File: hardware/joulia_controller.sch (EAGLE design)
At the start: 41 parts, among them IC1 LM2902D, IC2 LM2902D, U1 MMBT2222ALT1G, U2 MMBT2222ALT1G

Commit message: Complete wiring with HV circuit and rearrangement
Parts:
- renumbered U$3 to HE_HEATSINK, U$4 to P_HEATSINK
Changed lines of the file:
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@@
 <part name="U$1" library="digikey" deviceset="T3050H-6I" device=""/>
 <part name="U$2" library="digikey" deviceset="T3050H-6I" device=""/>
-<part name="U$3" library="digikey" deviceset="VM1-038-1AE" device=""/>
-<part name="U$4" library="digikey" deviceset="VM1-038-1AE" device=""/>
+<part name="HE_HEATSINK" library="digikey" deviceset="VM1-038-1AE" device=""/>
+<part name="P_HEATSINK" library="digikey" deviceset="VM1-038-1AE" device=""/>
 <part name="U$5" library="digikey" deviceset="MOC3020S" device=""/>
 <part name="U$6" library="digikey" deviceset="MOC3020S" device=""/>
@@
 <instance part="U$1" gate="G$1" x="292.1" y="124.46"/>
 <instance part="U$2" gate="G$1" x="292.1" y="76.2"/>
-<instance part="U$3" gate="G$1" x="309.88" y="124.46"/>
-<instance part="U$4" gate="G$1" x="309.88" y="76.2"/>
+<instance part="HE_HEATSINK" gate="G$1" x="309.88" y="124.46"/>
+<instance part="P_HEATSINK" gate="G$1" x="309.88" y="76.2"/>
 <instance part="U$5" gate="G$1" x="256.54" y="121.92"/>
 <instance part="U$6" gate="G$1" x="256.54" y="73.66"/>

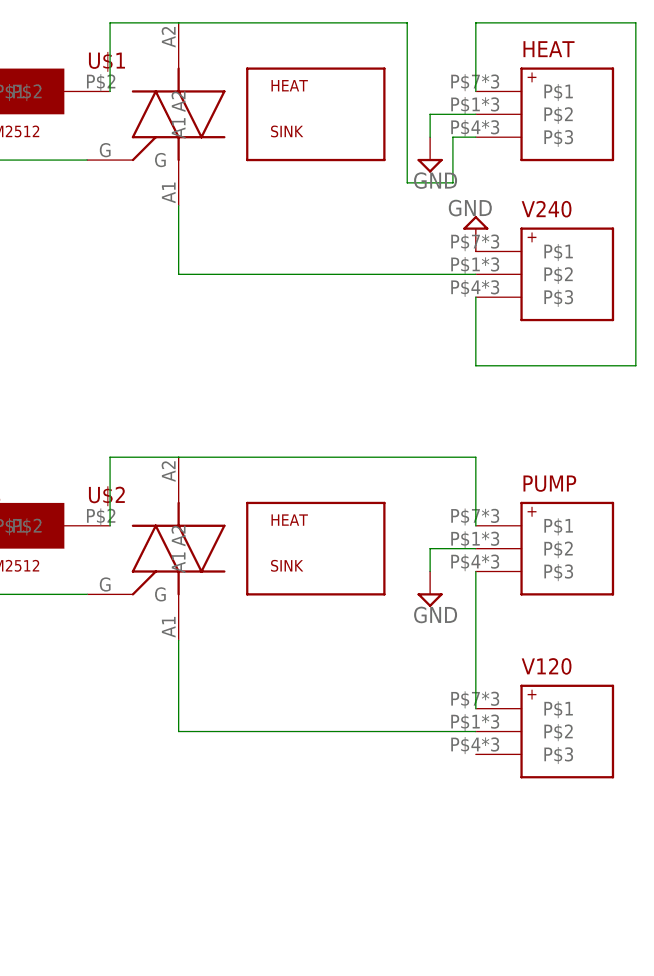
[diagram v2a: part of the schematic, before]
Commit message: Rewiring pump to be consistent with HE.
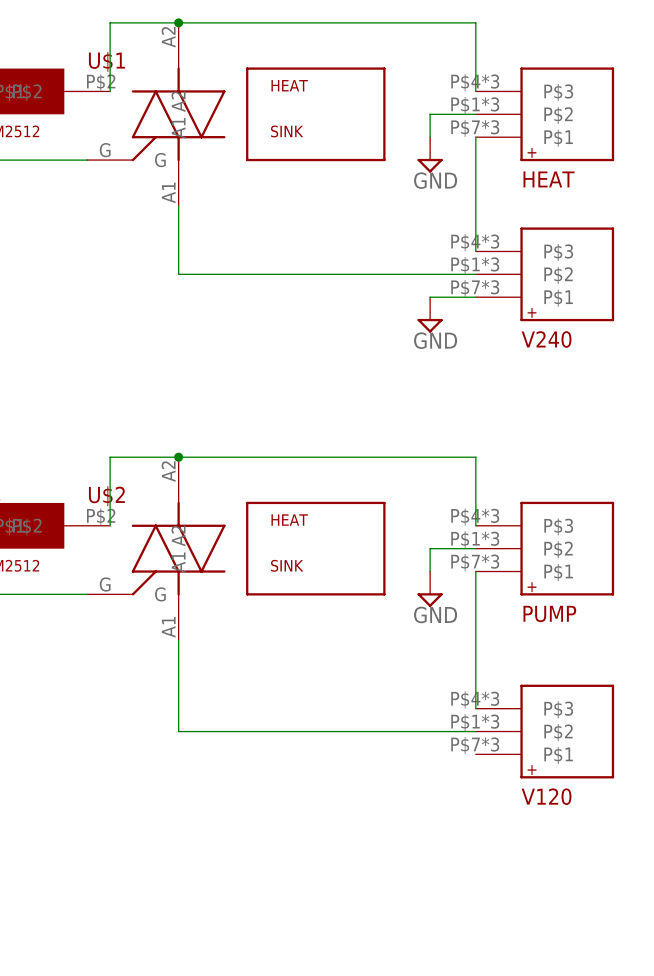
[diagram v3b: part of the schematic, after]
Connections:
- net N$26 renamed 120H
- net N$29 renamed +120
- net N$32 renamed -120
- removed net N$27: PUMP.P$3, V120.P$1
- new net 120N: PUMP.P$1, V120.P$3
- net N$24: now also PUMP.P$3; no longer PUMP.P$1
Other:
- moved on the sheet: HEAT, PUMP, V120, V240
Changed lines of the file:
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@@
 <instance part="P+1" gate="1" x="243.84" y="132.08"/>
 <instance part="P+2" gate="1" x="243.84" y="83.82"/>
-<instance part="HEAT" gate="G$1" x="332.74" y="124.46"/>
-<instance part="PUMP" gate="G$1" x="332.74" y="76.2"/>
+<instance part="HEAT" gate="G$1" x="332.74" y="124.46" rot="MR180"/>
+<instance part="PUMP" gate="G$1" x="332.74" y="76.2" rot="MR180"/>
 <instance part="SUPPLY17" gate="GND" x="322.58" y="119.38"/>
 <instance part="SUPPLY18" gate="GND" x="322.58" y="71.12"/>
-<instance part="V240" gate="G$1" x="332.74" y="106.68"/>
-<instance part="V120" gate="G$1" x="332.74" y="55.88"/>
-<instance part="SUPPLY19" gate="GND" x="327.66" y="111.76" rot="R180"/>
+<instance part="V240" gate="G$1" x="332.74" y="106.68" rot="MR180"/>
+<instance part="V120" gate="G$1" x="332.74" y="55.88" rot="MR180"/>
+<instance part="SUPPLY19" gate="GND" x="322.58" y="101.6"/>
 <instance part="R17" gate="G$1" x="243.84" y="111.76" rot="R90"/>
 <instance part="R18" gate="G$1" x="243.84" y="63.5" rot="R90"/>
@@
 <pinref part="V240" gate="G$1" pin="P$1"/>
 <pinref part="SUPPLY19" gate="GND" pin="GND"/>
+<wire x1="327.66" y1="104.14" x2="322.58" y2="104.14" width="0.1524" layer="91"/>
 </segment>
 </net>
@@
 <wire x1="287.02" y1="134.62" x2="294.64" y2="134.62" width="0.1524" layer="91"/>
 <pinref part="HEAT" gate="G$1" pin="P$3"/>
-<wire x1="327.66" y1="121.92" x2="325.12" y2="121.92" width="0.1524" layer="91"/>
-<wire x1="325.12" y1="121.92" x2="325.12" y2="116.84" width="0.1524" layer="91"/>
-<wire x1="325.12" y1="116.84" x2="320.04" y2="116.84" width="0.1524" layer="91"/>
-<wire x1="320.04" y1="116.84" x2="320.04" y2="134.62" width="0.1524" layer="91"/>
-<wire x1="320.04" y1="134.62" x2="294.64" y2="134.62" width="0.1524" layer="91"/>
+<wire x1="327.66" y1="127" x2="327.66" y2="134.62" width="0.1524" layer="91"/>
+<wire x1="327.66" y1="134.62" x2="294.64" y2="134.62" width="0.1524" layer="91"/>
+<junction x="294.64" y="134.62"/>
 </segment>
 </net>
@@
 <pinref part="U$2" gate="G$1" pin="A2"/>
 <wire x1="287.02" y1="86.36" x2="294.64" y2="86.36" width="0.1524" layer="91"/>
-<pinref part="PUMP" gate="G$1" pin="P$1"/>
-<wire x1="294.64" y1="86.36" x2="327.66" y2="86.36" width="0.1524" layer="91"/>
-<wire x1="327.66" y1="86.36" x2="327.66" y2="78.74" width="0.1524" layer="91"/>
-</segment>
-</net>
-<net name="N$26" class="1">
+<pinref part="PUMP" gate="G$1" pin="P$3"/>
+<wire x1="327.66" y1="78.74" x2="327.66" y2="86.36" width="0.1524" layer="91"/>
+<wire x1="327.66" y1="86.36" x2="294.64" y2="86.36" width="0.1524" layer="91"/>
+<junction x="294.64" y="86.36"/>
+</segment>
+</net>
+<net name="120H" class="1">
 <segment>
 <pinref part="U$2" gate="G$1" pin="A1"/>
@@
 </segment>
 </net>
-<net name="N$32" class="2">
+<net name="-120" class="2">
 <segment>
 <pinref part="V240" gate="G$1" pin="P$2"/>
@@
 </segment>
 </net>
-<net name="N$27" class="1">
-<segment>
-<pinref part="PUMP" gate="G$1" pin="P$3"/>
+<net name="+120" class="2">
+<segment>
+<pinref part="HEAT" gate="G$1" pin="P$1"/>
+<pinref part="V240" gate="G$1" pin="P$3"/>
+<wire x1="327.66" y1="121.92" x2="327.66" y2="109.22" width="0.1524" layer="91"/>
+</segment>
+</net>
+<net name="120N" class="1">
+<segment>
+<pinref part="PUMP" gate="G$1" pin="P$1"/>
+<pinref part="V120" gate="G$1" pin="P$3"/>
 <wire x1="327.66" y1="73.66" x2="327.66" y2="58.42" width="0.1524" layer="91"/>
-<pinref part="V120" gate="G$1" pin="P$1"/>
-</segment>
-</net>
-<net name="N$29" class="2">
-<segment>
-<pinref part="HEAT" gate="G$1" pin="P$1"/>
-<wire x1="327.66" y1="127" x2="327.66" y2="134.62" width="0.1524" layer="91"/>
-<wire x1="327.66" y1="134.62" x2="345.44" y2="134.62" width="0.1524" layer="91"/>
-<wire x1="345.44" y1="134.62" x2="345.44" y2="96.52" width="0.1524" layer="91"/>
-<pinref part="V240" gate="G$1" pin="P$3"/>
-<wire x1="345.44" y1="96.52" x2="327.66" y2="96.52" width="0.1524" layer="91"/>
-<wire x1="327.66" y1="96.52" x2="327.66" y2="104.14" width="0.1524" layer="91"/>
-</segment>
-</net>
+</segment>
+</net>

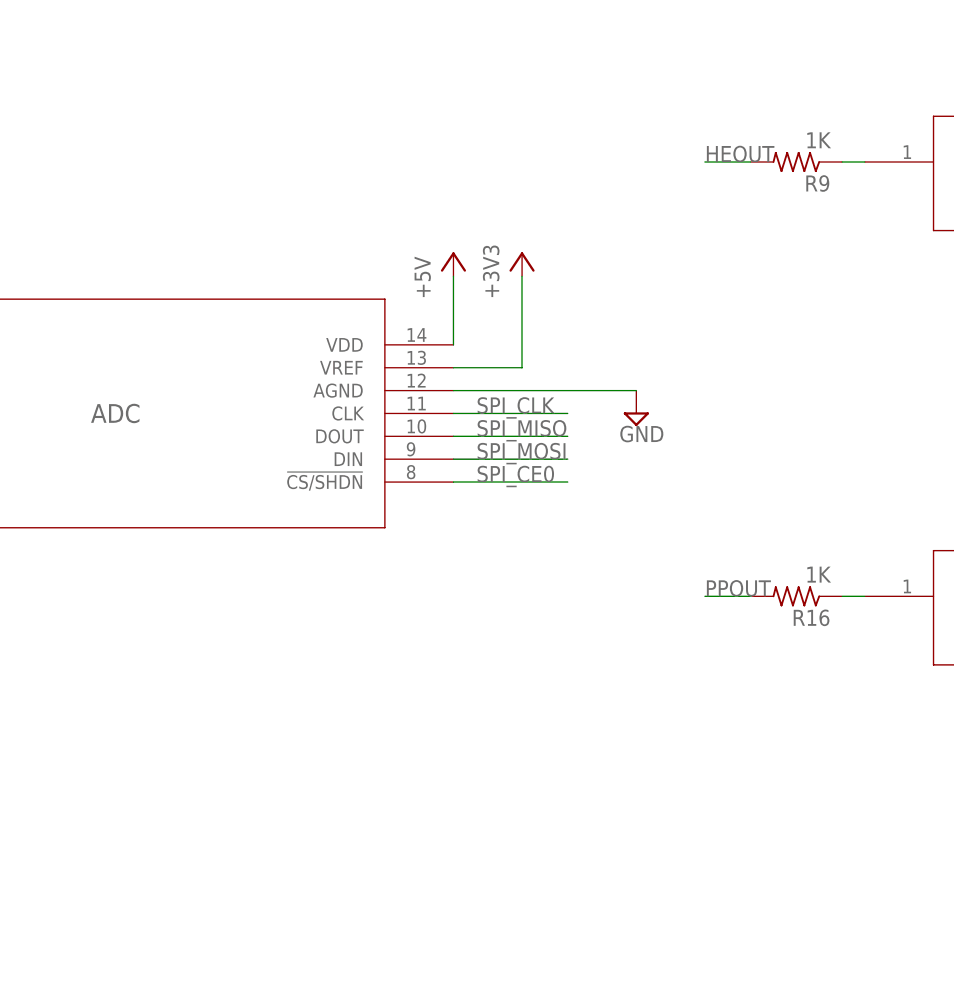
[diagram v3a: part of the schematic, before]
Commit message: Adding LEDs and Fan Connector
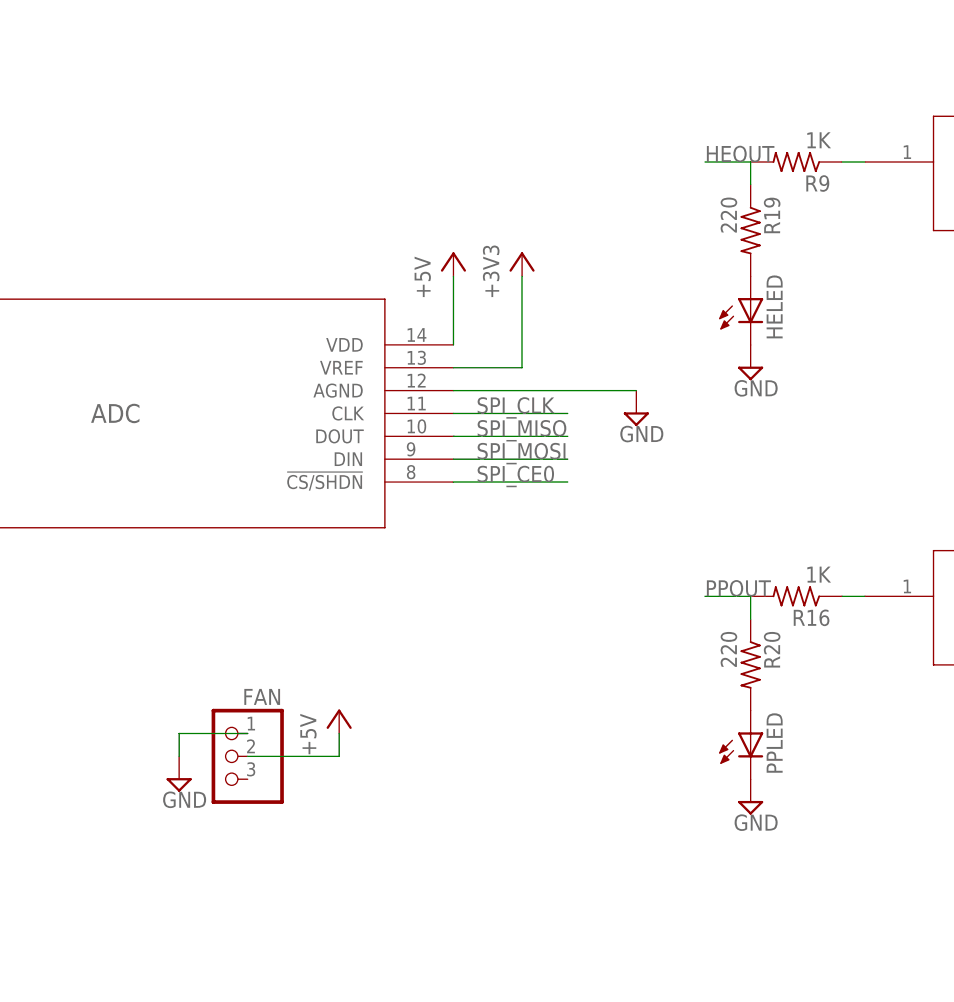
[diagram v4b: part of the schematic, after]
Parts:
- added FAN: (no value), adafruit:PINHD-1X3
- added HELED, PPLED: (no value), eagle-ltspice:LED_ESML0603
- added R19, R20: 220, rcl:R-US_R0402
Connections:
- new net N$25: HELED.A, R19.2
- new net N$26: PPLED.A, R20.2
- net +5V: now also FAN.2
- net GND: now also FAN.1, HELED.C, PPLED.C
- net HEOUT: now also R19.1
- net PPOUT: now also R20.1
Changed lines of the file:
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@@
 <part name="R17" library="resistor" library_urn="urn:adsk.eagle:library:348" deviceset="R-US_" device="R1206" value="330"/>
 <part name="R18" library="resistor" library_urn="urn:adsk.eagle:library:348" deviceset="R-US_" device="R1206" value="330"/>
+<part name="HELED" library="eagle-ltspice" library_urn="urn:adsk.eagle:library:217" deviceset="LED_E" device="SML0603"/>
+<part name="PPLED" library="eagle-ltspice" library_urn="urn:adsk.eagle:library:217" deviceset="LED_E" device="SML0603"/>
+<part name="R19" library="rcl" library_urn="urn:adsk.eagle:library:334" deviceset="R-US_" device="R0402" value="220"/>
+<part name="SUPPLY20" library="supply2" deviceset="GND" device=""/>
+<part name="SUPPLY21" library="supply2" deviceset="GND" device=""/>
+<part name="R20" library="rcl" library_urn="urn:adsk.eagle:library:334" deviceset="R-US_" device="R0402" value="220"/>
+<part name="FAN" library="adafruit" deviceset="PINHD-1X3" device=""/>
+<part name="SUPPLY22" library="supply2" deviceset="GND" device=""/>
+<part name="P+8" library="supply1" library_urn="urn:adsk.eagle:library:371" deviceset="+5V" device=""/>
 </parts>
 <sheets>
@@
 <instance part="R17" gate="G$1" x="243.84" y="111.76" rot="R90"/>
 <instance part="R18" gate="G$1" x="243.84" y="63.5" rot="R90"/>
+<instance part="HELED" gate="G$1" x="185.42" y="88.9"/>
+<instance part="PPLED" gate="G$1" x="185.42" y="40.64"/>
+<instance part="R19" gate="G$1" x="185.42" y="96.52" rot="R270"/>
+<instance part="SUPPLY20" gate="GND" x="185.42" y="81.28"/>
+<instance part="SUPPLY21" gate="GND" x="185.42" y="33.02"/>
+<instance part="R20" gate="G$1" x="185.42" y="48.26" rot="R270"/>
+<instance part="FAN" gate="A" x="127" y="38.1" rot="MR0"/>
+<instance part="SUPPLY22" gate="GND" x="121.92" y="35.56"/>
+<instance part="P+8" gate="1" x="139.7" y="43.18"/>
 </instances>
 <busses>
@@
 <wire x1="327.66" y1="104.14" x2="322.58" y2="104.14" width="0.1524" layer="91"/>
 </segment>
+<segment>
+<pinref part="HELED" gate="G$1" pin="C"/>
+<pinref part="SUPPLY20" gate="GND" pin="GND"/>
+</segment>
+<segment>
+<pinref part="PPLED" gate="G$1" pin="C"/>
+<pinref part="SUPPLY21" gate="GND" pin="GND"/>
+</segment>
+<segment>
+<pinref part="SUPPLY22" gate="GND" pin="GND"/>
+<wire x1="121.92" y1="38.1" x2="121.92" y2="40.64" width="0.1524" layer="91"/>
+<pinref part="FAN" gate="A" pin="1"/>
+<wire x1="121.92" y1="40.64" x2="129.54" y2="40.64" width="0.1524" layer="91"/>
+</segment>
 </net>
 <net name="N$4" class="0">
@@
 <wire x1="243.84" y1="129.54" x2="243.84" y2="127" width="0.1524" layer="91"/>
 </segment>
+<segment>
+<pinref part="P+8" gate="1" pin="+5V"/>
+<wire x1="139.7" y1="40.64" x2="139.7" y2="38.1" width="0.1524" layer="91"/>
+<pinref part="FAN" gate="A" pin="2"/>
+<wire x1="139.7" y1="38.1" x2="129.54" y2="38.1" width="0.1524" layer="91"/>
+</segment>
 </net>
 <net name="+3V3" class="0">
@@
 <label x="180.34" y="104.14" size="1.778" layer="95"/>
 <wire x1="185.42" y1="104.14" x2="180.34" y2="104.14" width="0.1524" layer="91"/>
+<pinref part="R19" gate="G$1" pin="1"/>
+<wire x1="185.42" y1="101.6" x2="185.42" y2="104.14" width="0.1524" layer="91"/>
 </segment>
 </net>
@@
 <label x="180.34" y="55.88" size="1.778" layer="95"/>
 <wire x1="185.42" y1="55.88" x2="180.34" y2="55.88" width="0.1524" layer="91"/>
+<pinref part="R20" gate="G$1" pin="1"/>
+<wire x1="185.42" y1="53.34" x2="185.42" y2="55.88" width="0.1524" layer="91"/>
 </segment>
 </net>
@@
 </segment>
 </net>
+<net name="N$25" class="0">
+<segment>
+<pinref part="HELED" gate="G$1" pin="A"/>
+<pinref part="R19" gate="G$1" pin="2"/>
+</segment>
+</net>
+<net name="N$26" class="0">
+<segment>
+<pinref part="R20" gate="G$1" pin="2"/>
+<pinref part="PPLED" gate="G$1" pin="A"/>
+</segment>
+</net>
